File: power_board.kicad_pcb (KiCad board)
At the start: 4 copper layers, 23.2 x 11.2 mm, 14 parts, among them J1 CONN_01X05, P1 BATT, Q1 DMP1045U, U1 MCP73831T-2ACI_OT, U7 MH2mm

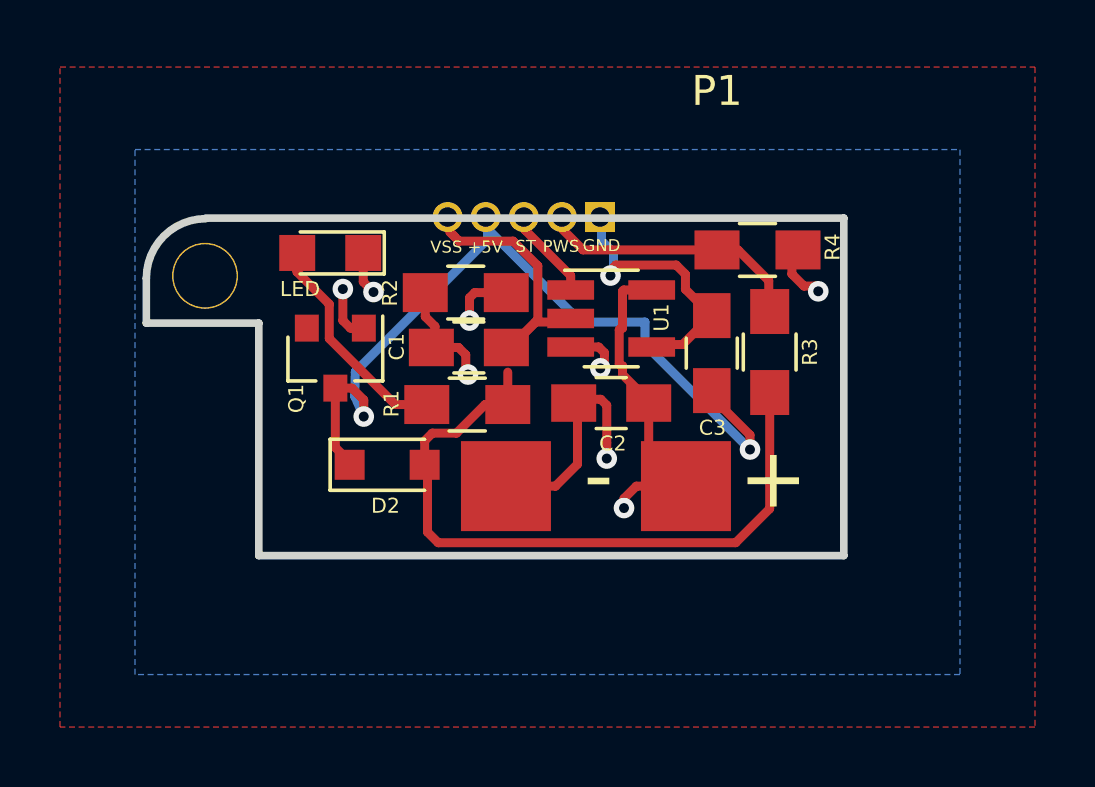
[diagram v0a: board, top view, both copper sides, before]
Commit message: Update for LIPO power_board
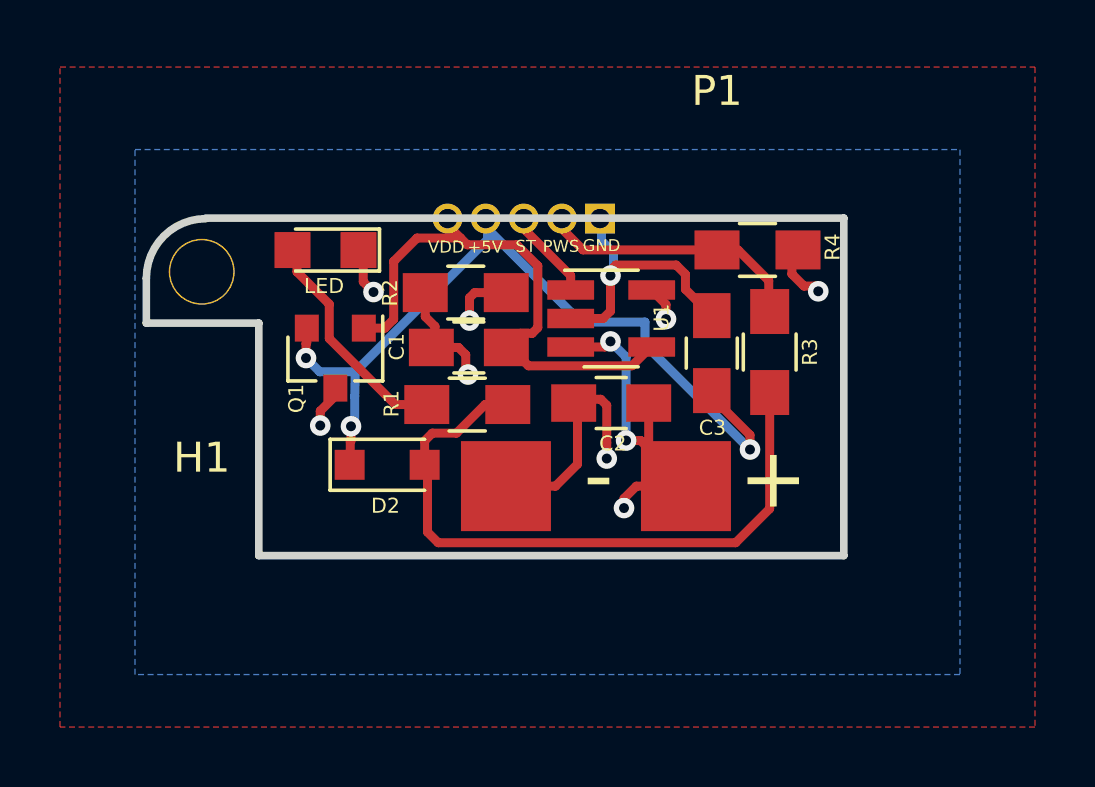
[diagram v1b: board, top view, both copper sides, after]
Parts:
- removed U7: MH2mm, my-fp-library:MH2.1mm
- added H1: MH2.1mm, my-fp-library:MH2.1mm, F.Cu at (149.7, 111.6)
- Q1: value DMP1045U -> Q_PMOS_GSD (DMP1045U)
- moved LED 0.19 mm to (153.8, 110.8)
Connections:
- C1 pad 1: VSS -> VDD
- C2 pad 1: Net-(C2-Pad1) -> /D
- D2 pad 2: VSS -> VDD
- J1 pad 5: VSS -> VDD
- P1 pad 1: Net-(C2-Pad1) -> /D
- Q1 pad 1: Net-(C2-Pad1) -> VDD
- Q1 pad 2: VSS -> +5V
- Q1 pad 3: +5V -> /D
- R1 pad 1: VSS -> VDD
- R3 pad 2: VSS -> VDD
- U1 pad 2: VSS -> (GND)
- U1 pad 3: Net-(R2-Pad1) -> /D
- U1 pad 4: (GND) -> VDD
- U1 pad 5: Net-(C2-Pad1) -> Net-(R2-Pad1)
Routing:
- net VDD: track 0.00 -> 40.2 mm
- net VSS: track 32.9 -> 0.00 mm
- net Net-(C2-Pad1): track 31.6 -> 0.00 mm, vias 2 -> 0
- net /D: track 0.00 -> 27.8 mm, vias 0 -> 4
- net Net-(R2-Pad1): track 8.77 -> 11.4 mm
- net (GND): track 23.1 -> 22.2 mm
- net +5V: track 27.4 -> 27.2 mm, vias 2 -> 3
- added copper zone on F.Cu, net VDD
- removed copper zone on F.Cu, net VSS
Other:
- board text added: "VDD"
- board text removed: "VSS"
